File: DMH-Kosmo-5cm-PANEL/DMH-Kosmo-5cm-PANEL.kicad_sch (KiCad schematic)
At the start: 5 parts, among them J0 Panel_GND_Solder_Wire_Pad

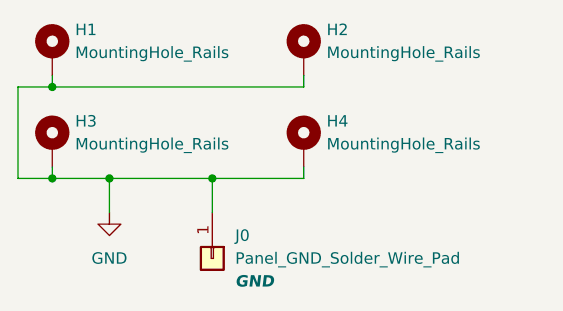
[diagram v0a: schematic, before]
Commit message: Matched main PCB size reference in PANEL templates
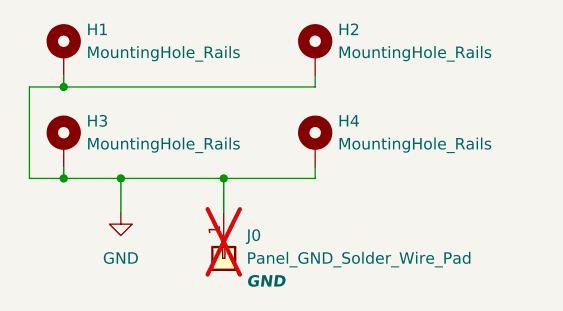
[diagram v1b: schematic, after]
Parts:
- J0: now not fitted
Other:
- moved on the sheet: H1, H2, H3, H4
